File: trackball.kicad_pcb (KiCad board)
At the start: 2 copper layers, 27.5 x 35.2 mm, 38 parts, among them P1 CONN_10, P2 CONN_5, U1 MKL03Z32VFK4, U2 ADNS-3530, U4 ESD

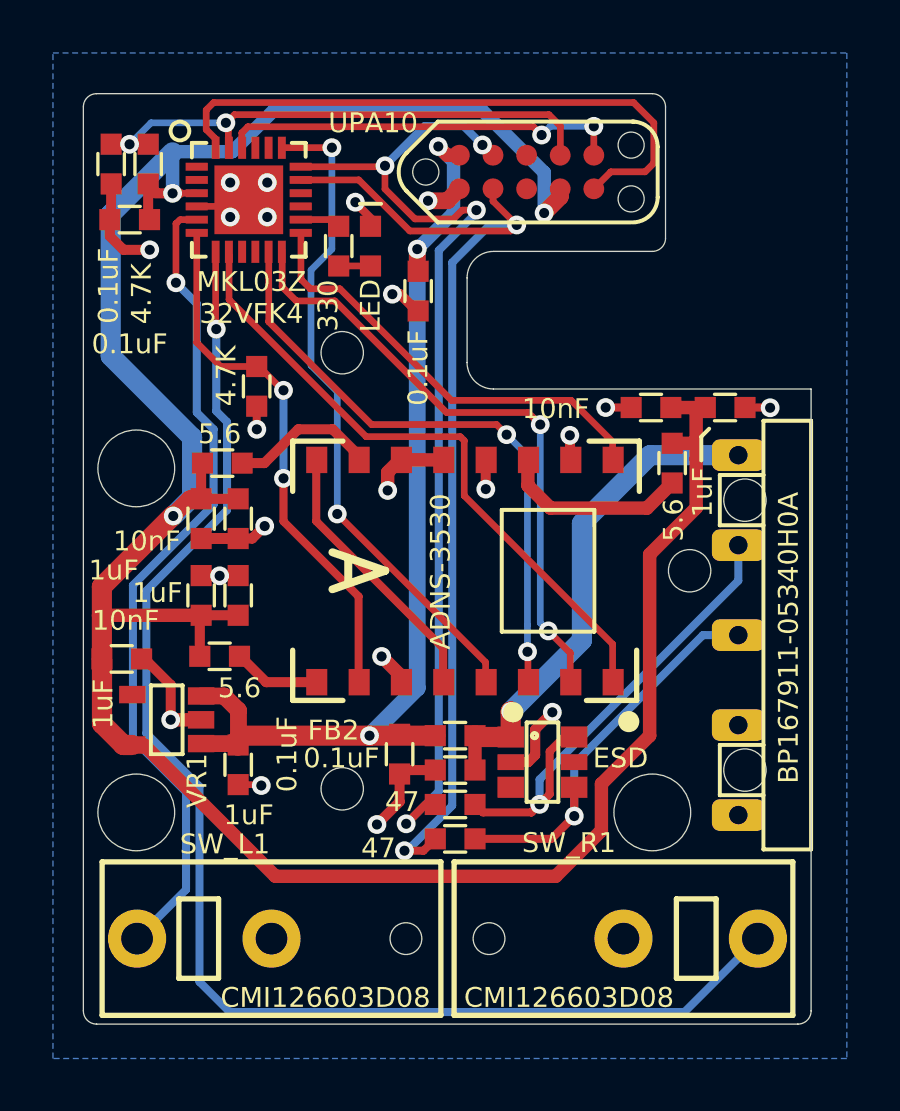
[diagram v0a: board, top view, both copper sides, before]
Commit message: Fix sensor position.
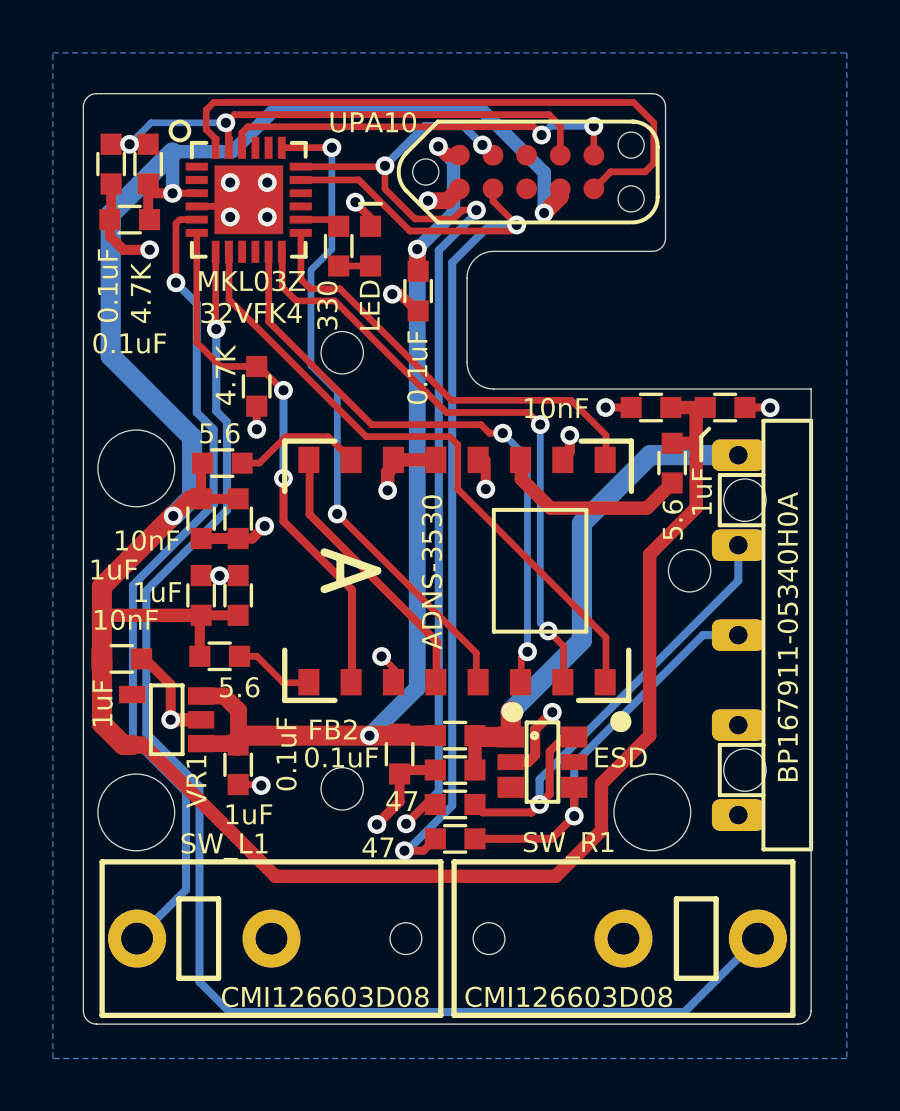
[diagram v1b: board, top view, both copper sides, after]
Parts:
- moved U2 0.30 mm to (196.3, 130.6)
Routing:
- net Net-(R8-Pad1): track 5.51 -> 4.80 mm
- net /MISO: track 24.4 -> 23.7 mm
- net Net-(U2-Pad5): track 10.6 -> 9.89 mm
- net GND: track 35.7 -> 35.1 mm
- net /SHTDWN: track 20.6 -> 20.0 mm

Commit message: Update sensor footprint.
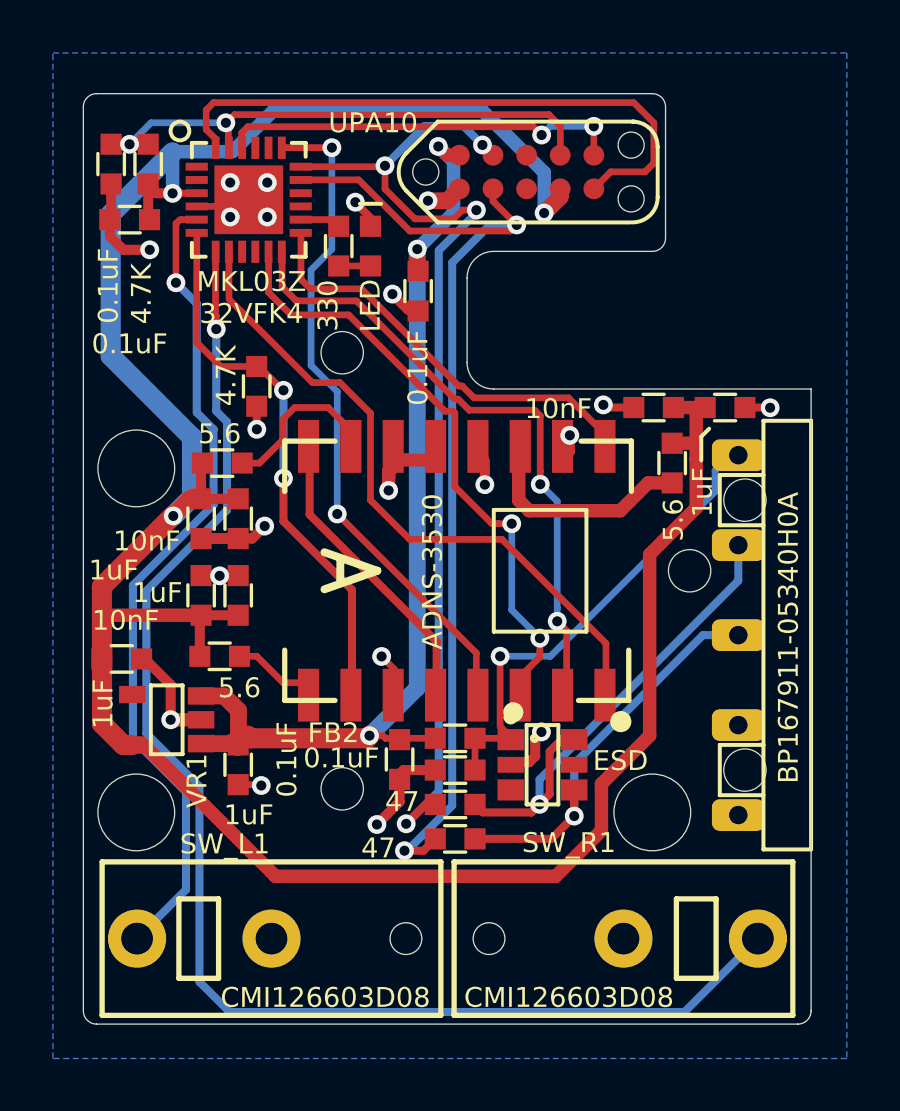
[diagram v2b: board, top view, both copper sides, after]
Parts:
- moved C8 0.20 mm to (194.1, 137.7)
- moved C9 0.10 mm to (203.7, 124.4)
- moved FB2 0.10 mm to (196.2, 136.9)
- moved U4 0.10 mm to (199.5, 137.9)
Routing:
- net /VCC_BOTTOM: track 19.2 -> 17.7 mm
- net GND: track 35.1 -> 34.3 mm
- net Net-(R8-Pad1): track 4.80 -> 5.56 mm
- net /MISO: track 23.7 -> 24.4 mm
- net Net-(R5-Pad1): track 7.02 -> 7.71 mm
- net /MOSI: track 23.0 -> 22.4 mm

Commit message: Update sensor footprint.
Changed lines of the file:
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@@
   (general
     (thickness 1.6)
-    (drawings 46)
+    (drawings 45)
     (tracks 399)
     (zones 0)
@@
       (effects (font (size 0.746 0.746) (thickness 0.15)) (justify mirror))
     )
-    (fp_text value ADNS-3530 (at 0.910001 -0.030997 90) (layer F.SilkS)
-      (effects (font (size 0.75 0.75) (thickness 0.15)))
-    )
+    (fp_text value ADNS-3530 (at -0.939999 -0.030997 90 unlocked) (layer F.SilkS)
+      (effects (font (size 0.75 0.75) (thickness 0.15)))
+    )
+    (fp_line (start -4.35 -0.4) (end -4.35 0.4) (layer F.SilkS) (width 0.3))
+    (fp_line (start -2.95 0) (end -4.95 -0.7) (layer F.SilkS) (width 0.3))
+    (fp_line (start -4.95 0.7) (end -2.95 0) (layer F.SilkS) (width 0.3))
+    (fp_line (start 1.4 2.3) (end 4.9 2.3) (layer F.SilkS) (width 0.15))
+    (fp_line (start 1.4 -2.3) (end 4.9 -2.3) (layer F.SilkS) (width 0.15))
+    (fp_line (start 4.9 -2.3) (end 4.9 2.3) (layer F.SilkS) (width 0.15))
+    (fp_line (start 1.4 -2.3) (end 1.4 2.3) (layer F.SilkS) (width 0.15))
+    (fp_circle (center -6.2 -5.7) (end -6 -5.7) (layer F.SilkS) (width 0.4))
+    (fp_line (start 6.5 4.9) (end 4.6 4.9) (layer F.SilkS) (width 0.2))
+    (fp_line (start 6.5 4.9) (end 6.5 3) (layer F.SilkS) (width 0.2))
+    (fp_line (start 6.5 -4.9) (end 6.5 -3) (layer F.SilkS) (width 0.2))
+    (fp_line (start 6.5 -4.9) (end 4.6 -4.9) (layer F.SilkS) (width 0.2))
+    (fp_line (start -6.6 4.9) (end -6.6 3) (layer F.SilkS) (width 0.2))
+    (fp_line (start -6.6 4.9) (end -4.7 4.9) (layer F.SilkS) (width 0.2))
+    (fp_line (start -6.5 -4.9) (end -6.5 -3) (layer F.SilkS) (width 0.2))
     (fp_line (start -6.5 -4.9) (end -4.6 -4.9) (layer F.SilkS) (width 0.2))
-    (fp_line (start -6.5 -4.9) (end -6.5 -3) (layer F.SilkS) (width 0.2))
-    (fp_line (start -6.6 4.9) (end -4.7 4.9) (layer F.SilkS) (width 0.2))
-    (fp_line (start -6.6 4.9) (end -6.6 3) (layer F.SilkS) (width 0.2))
-    (fp_line (start 6.5 -4.9) (end 4.6 -4.9) (layer F.SilkS) (width 0.2))
-    (fp_line (start 6.5 -4.9) (end 6.5 -3) (layer F.SilkS) (width 0.2))
-    (fp_line (start 6.5 4.9) (end 6.5 3) (layer F.SilkS) (width 0.2))
-    (fp_line (start 6.5 4.9) (end 4.6 4.9) (layer F.SilkS) (width 0.2))
-    (fp_circle (center -6.2 -5.7) (end -6 -5.7) (layer F.SilkS) (width 0.4))
-    (fp_line (start -4.9 -2.3) (end -4.9 2.3) (layer F.SilkS) (width 0.15))
-    (fp_line (start -1.4 -2.3) (end -1.4 2.3) (layer F.SilkS) (width 0.15))
-    (fp_line (start -4.9 -2.3) (end -1.4 -2.3) (layer F.SilkS) (width 0.15))
-    (fp_line (start -4.9 2.3) (end -1.4 2.3) (layer F.SilkS) (width 0.15))
-    (fp_line (start 5 -0.7) (end 3 0) (layer F.SilkS) (width 0.3))
-    (fp_line (start 3 0) (end 5 0.7) (layer F.SilkS) (width 0.3))
-    (fp_line (start 4.4 0.4) (end 4.4 -0.4) (layer F.SilkS) (width 0.3))
     (fp_text user A (at 0.160001 0.019003 270) (layer F.SilkS) hide
       (effects (font (size 2 2) (thickness 0.3)) (justify mirror))
     )
+    (pad 9 smd rect (at 5.6 4.7 180) (size 0.8 2) (layers F.Cu F.Mask)
+      (net 9 "Net-(U2-Pad5)"))
+    (pad 10 smd rect (at 4 4.7 180) (size 0.8 2) (layers F.Cu F.Mask)
+      (net 14 "Net-(R8-Pad1)"))
+    (pad 11 smd rect (at 2.4 4.7 180) (size 0.8 2) (layers F.Cu F.Mask)
+      (net 1 GND))
+    (pad 12 smd rect (at 0.8 4.7 180) (size 0.8 2) (layers F.Cu F.Mask)
+      (net 1 GND))
+    (pad 13 smd rect (at -0.8 4.7 180) (size 0.8 2) (layers F.Cu F.Mask)
+      (net 1 GND))
+    (pad 14 smd rect (at -2.4 4.7 180) (size 0.8 2) (layers F.Cu F.Mask)
+      (net 15 "Net-(R5-Pad1)"))
+    (pad 15 smd rect (at -4 4.7 180) (size 0.8 2) (layers F.Cu F.Mask)
+      (net 1 GND))
+    (pad 16 smd rect (at -5.6 4.7 180) (size 0.8 2) (layers F.Cu F.Mask)
+      (net 16 /NCS))
+    (pad 8 smd rect (at 5.6 -4.7 180) (size 0.8 2) (layers F.Cu F.Mask)
+      (net 7 "Net-(R3-Pad1)"))
+    (pad 7 smd rect (at 4 -4.7 180) (size 0.8 2) (layers F.Cu F.Mask)
+      (net 8 /SHTDWN))
+    (pad 6 smd rect (at 2.4 -4.7 180) (size 0.8 2) (layers F.Cu F.Mask)
+      (net 1 GND))
+    (pad 5 smd rect (at 0.8 -4.7 180) (size 0.8 2) (layers F.Cu F.Mask)
+      (net 9 "Net-(U2-Pad5)"))
+    (pad 4 smd rect (at -0.8 -4.7 180) (size 0.8 2) (layers F.Cu F.Mask)
+      (net 10 /MOTION))
+    (pad 3 smd rect (at -2.4 -4.7 180) (size 0.8 2) (layers F.Cu F.Mask)
+      (net 11 /MOSI))
+    (pad 2 smd rect (at -4 -4.7 180) (size 0.8 2) (layers F.Cu F.Mask)
+      (net 12 /SCK))
     (pad 1 smd rect (at -5.6 -4.7 180) (size 0.8 2) (layers F.Cu F.Mask)
       (net 13 /MISO))
-    (pad 2 smd rect (at -4 -4.7 180) (size 0.8 2) (layers F.Cu F.Mask)
-      (net 12 /SCK))
-    (pad 3 smd rect (at -2.4 -4.7 180) (size 0.8 2) (layers F.Cu F.Mask)
-      (net 11 /MOSI))
-    (pad 4 smd rect (at -0.8 -4.7 180) (size 0.8 2) (layers F.Cu F.Mask)
-      (net 10 /MOTION))
-    (pad 5 smd rect (at 0.8 -4.7 180) (size 0.8 2) (layers F.Cu F.Mask)
-      (net 9 "Net-(U2-Pad5)"))
-    (pad 6 smd rect (at 2.4 -4.7 180) (size 0.8 2) (layers F.Cu F.Mask)
-      (net 1 GND))
-    (pad 7 smd rect (at 4 -4.7 180) (size 0.8 2) (layers F.Cu F.Mask)
-      (net 8 /SHTDWN))
-    (pad 8 smd rect (at 5.6 -4.7 180) (size 0.8 2) (layers F.Cu F.Mask)
-      (net 7 "Net-(R3-Pad1)"))
-    (pad 16 smd rect (at -5.6 4.7 180) (size 0.8 2) (layers F.Cu F.Mask)
-      (net 16 /NCS))
-    (pad 15 smd rect (at -4 4.7 180) (size 0.8 2) (layers F.Cu F.Mask)
-      (net 1 GND))
-    (pad 14 smd rect (at -2.4 4.7 180) (size 0.8 2) (layers F.Cu F.Mask)
-      (net 15 "Net-(R5-Pad1)"))
-    (pad 13 smd rect (at -0.8 4.7 180) (size 0.8 2) (layers F.Cu F.Mask)
-      (net 1 GND))
-    (pad 12 smd rect (at 0.8 4.7 180) (size 0.8 2) (layers F.Cu F.Mask)
-      (net 1 GND))
-    (pad 11 smd rect (at 2.4 4.7 180) (size 0.8 2) (layers F.Cu F.Mask)
-      (net 1 GND))
-    (pad 10 smd rect (at 4 4.7 180) (size 0.8 2) (layers F.Cu F.Mask)
-      (net 14 "Net-(R8-Pad1)"))
-    (pad 9 smd rect (at 5.6 4.7 180) (size 0.8 2) (layers F.Cu F.Mask)
-      (net 9 "Net-(U2-Pad5)"))
   )
   (module ugl:SM0603_Diode (layer F.Cu)
@@
       (effects (font (size 0.75 0.75) (thickness 0.15)))
     )
+    (fp_circle (center -1.8 1.2) (end -1.6 1.2) (layer F.SilkS) (width 0.15))
+    (fp_circle (center -1 0.3) (end -0.9 0.3) (layer F.SilkS) (width 0.15))
+    (fp_line (start -1.5 0.6) (end -1.5 -0.6) (layer F.SilkS) (width 0.15))
+    (fp_line (start 1.5 0.6) (end -1.5 0.6) (layer F.SilkS) (width 0.15))
+    (fp_line (start 1.5 -0.6) (end 1.5 0.6) (layer F.SilkS) (width 0.15))
     (fp_line (start -1.5 -0.6) (end 1.5 -0.6) (layer F.SilkS) (width 0.15))
-    (fp_line (start 1.5 -0.6) (end 1.5 0.6) (layer F.SilkS) (width 0.15))
-    (fp_line (start 1.5 0.6) (end -1.5 0.6) (layer F.SilkS) (width 0.15))
-    (fp_line (start -1.5 0.6) (end -1.5 -0.6) (layer F.SilkS) (width 0.15))
-    (fp_circle (center -1 0.3) (end -0.9 0.3) (layer F.SilkS) (width 0.15))
-    (fp_circle (center -1.8 1.2) (end -1.6 1.2) (layer F.SilkS) (width 0.15))
-    (pad 3 smd rect (at 0.95 1.2 270) (size 0.8 1) (layers F.Cu F.Paste F.Mask))
-    (pad 2 smd rect (at 0 1.2 270) (size 0.6 1) (layers F.Cu F.Paste F.Mask)
-      (net 1 GND))
+    (pad "" smd rect (at 0 -1.2 270) (size 0.6 1) (layers F.Cu F.Paste F.Mask))
+    (pad 5 smd rect (at -0.95 -1.2 270) (size 0.8 1) (layers F.Cu F.Paste F.Mask)
+      (net 3 /SDA_BOTTOM))
+    (pad 4 smd rect (at 0.95 -1.2 270) (size 0.8 1) (layers F.Cu F.Paste F.Mask)
+      (net 2 /SCL_BOTTOM))
     (pad 1 smd rect (at -0.95 1.2 270) (size 0.8 1) (layers F.Cu F.Paste F.Mask)
       (net 4 /VCC_BOTTOM))
-    (pad 4 smd rect (at 0.95 -1.2 270) (size 0.8 1) (layers F.Cu F.Paste F.Mask)
-      (net 2 /SCL_BOTTOM))
-    (pad 5 smd rect (at -0.95 -1.2 270) (size 0.8 1) (layers F.Cu F.Paste F.Mask)
-      (net 3 /SDA_BOTTOM))
-    (pad "" smd rect (at 0 -1.2 270) (size 0.6 1) (layers F.Cu F.Paste F.Mask))
+    (pad 2 smd rect (at 0 1.2 270) (size 0.6 1) (layers F.Cu F.Paste F.Mask)
+      (net 1 GND))
+    (pad 3 smd rect (at 0.95 1.2 270) (size 0.8 1) (layers F.Cu F.Paste F.Mask))
   )
   (module ugl:SM0603 (layer F.Cu)
@@
       (net 4 /VCC_BOTTOM) (clearance 0.0762))
   )
-  (dimension 14.410001 (width 0.15) (layer F.SilkS)
-    (gr_text "14.410 mm" (at 189.355 149.42) (layer F.SilkS)
-      (effects (font (size 0.75 0.75) (thickness 0.15)))
-    )
-    (feature1 (pts (xy 182.15 130.569003) (xy 182.15 148.956421)))
-    (feature2 (pts (xy 196.560001 130.569003) (xy 196.560001 148.956421)))
-    (crossbar (pts (xy 196.560001 148.37) (xy 182.15 148.37)))
-    (arrow1a (pts (xy 182.15 148.37) (xy 183.276504 147.783579)))
-    (arrow1b (pts (xy 182.15 148.37) (xy 183.276504 148.956421)))
-    (arrow2a (pts (xy 196.560001 148.37) (xy 195.433497 147.783579)))
-    (arrow2b (pts (xy 196.560001 148.37) (xy 195.433497 148.956421)))
-  )
   (gr_circle (center 198.397133 135.916091) (end 198.577411 135.916091) (layer F.SilkS) (width 0.4))
